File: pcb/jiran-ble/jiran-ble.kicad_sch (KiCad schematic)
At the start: 167 parts, among them J1 BATT, J2 USB-C Connector, J3 SWD, J4 BATT, J5 USB-C Connector, J6 SWD, Q1 SI2301CDS-T1-GE3, Q2 SI2301CDS-T1-GE3, SW1 SW_DPDT_x2, SW10 SW_Push, SW11 SW_Push, SW12 SW_Push, SW13 SW_Push, SW14 SW_Push, SW15 SW_Push, SW16 SW_Push, SW17 SW_Push, SW18 SW_Push, SW19 SW_Push, SW2 SW_Push, SW20 SW_Push, SW21 SW_Push, SW22 SW_Push, SW23 SW_Push, SW24 SW_Push, SW25 SW_Push, SW26 SW_Push, SW27 SW_Push, SW28 SW_Push, SW29 SW_Push, SW3 SW_Push, SW30 SW_Push, SW31 SW_Push, SW32 SW_Push, SW33 SW_Push, SW34 SW_Push, SW35 SW_Push, SW36 SW_Push, SW37 SW_Push, SW38 SW_Push, SW39 SW_Push, SW4 SW_Push, SW40 SW_Push, SW41 SW_Push, SW42 SW_Push, SW43 SW_Push, SW44 SW_Push, SW45 SW_Push, SW46 SW_Push, SW47 SW_Push, SW48 SW_Push, SW49 SW_Push, SW5 SW_Push, SW50 SW_Push, SW51 SW_Push, SW52 SW_Push, SW53 SW_Push, SW54 SW_Push, SW55 SW_Push, SW56 SW_Push, SW57 SW_Push, SW58 SW_Push, SW59 SW_Push, SW6 SW_Push, SW7 SW_Push, SW8 SW_Push, SW9 SW_Push, U1 HOLYIOT-18010-NRF52840_simple, U2 XC6220B331MR-G, U3 TP4054, U4 HOLYIOT-18010-NRF52840_simple, U5 XC6220B331MR-G, U6 TP4054

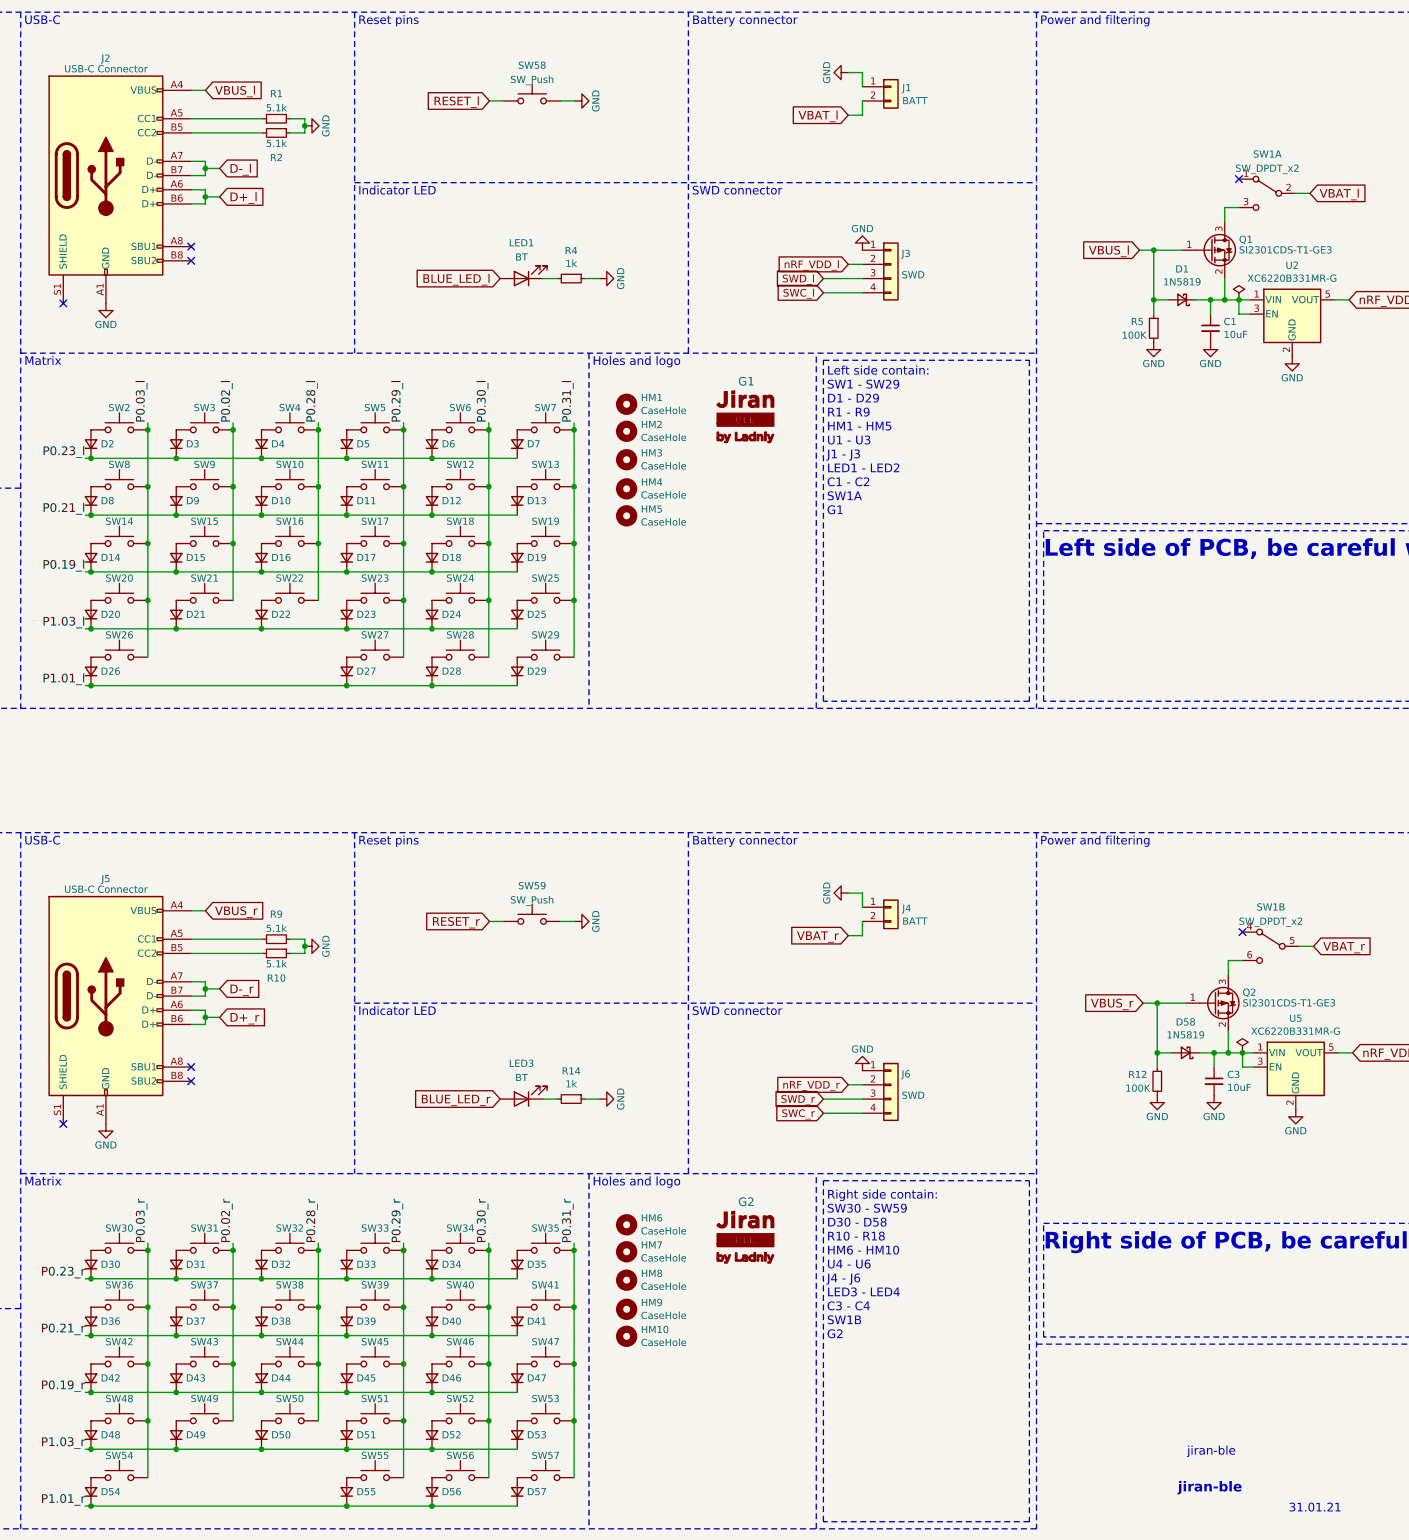
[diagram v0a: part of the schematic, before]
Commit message: Change DPDT symbol
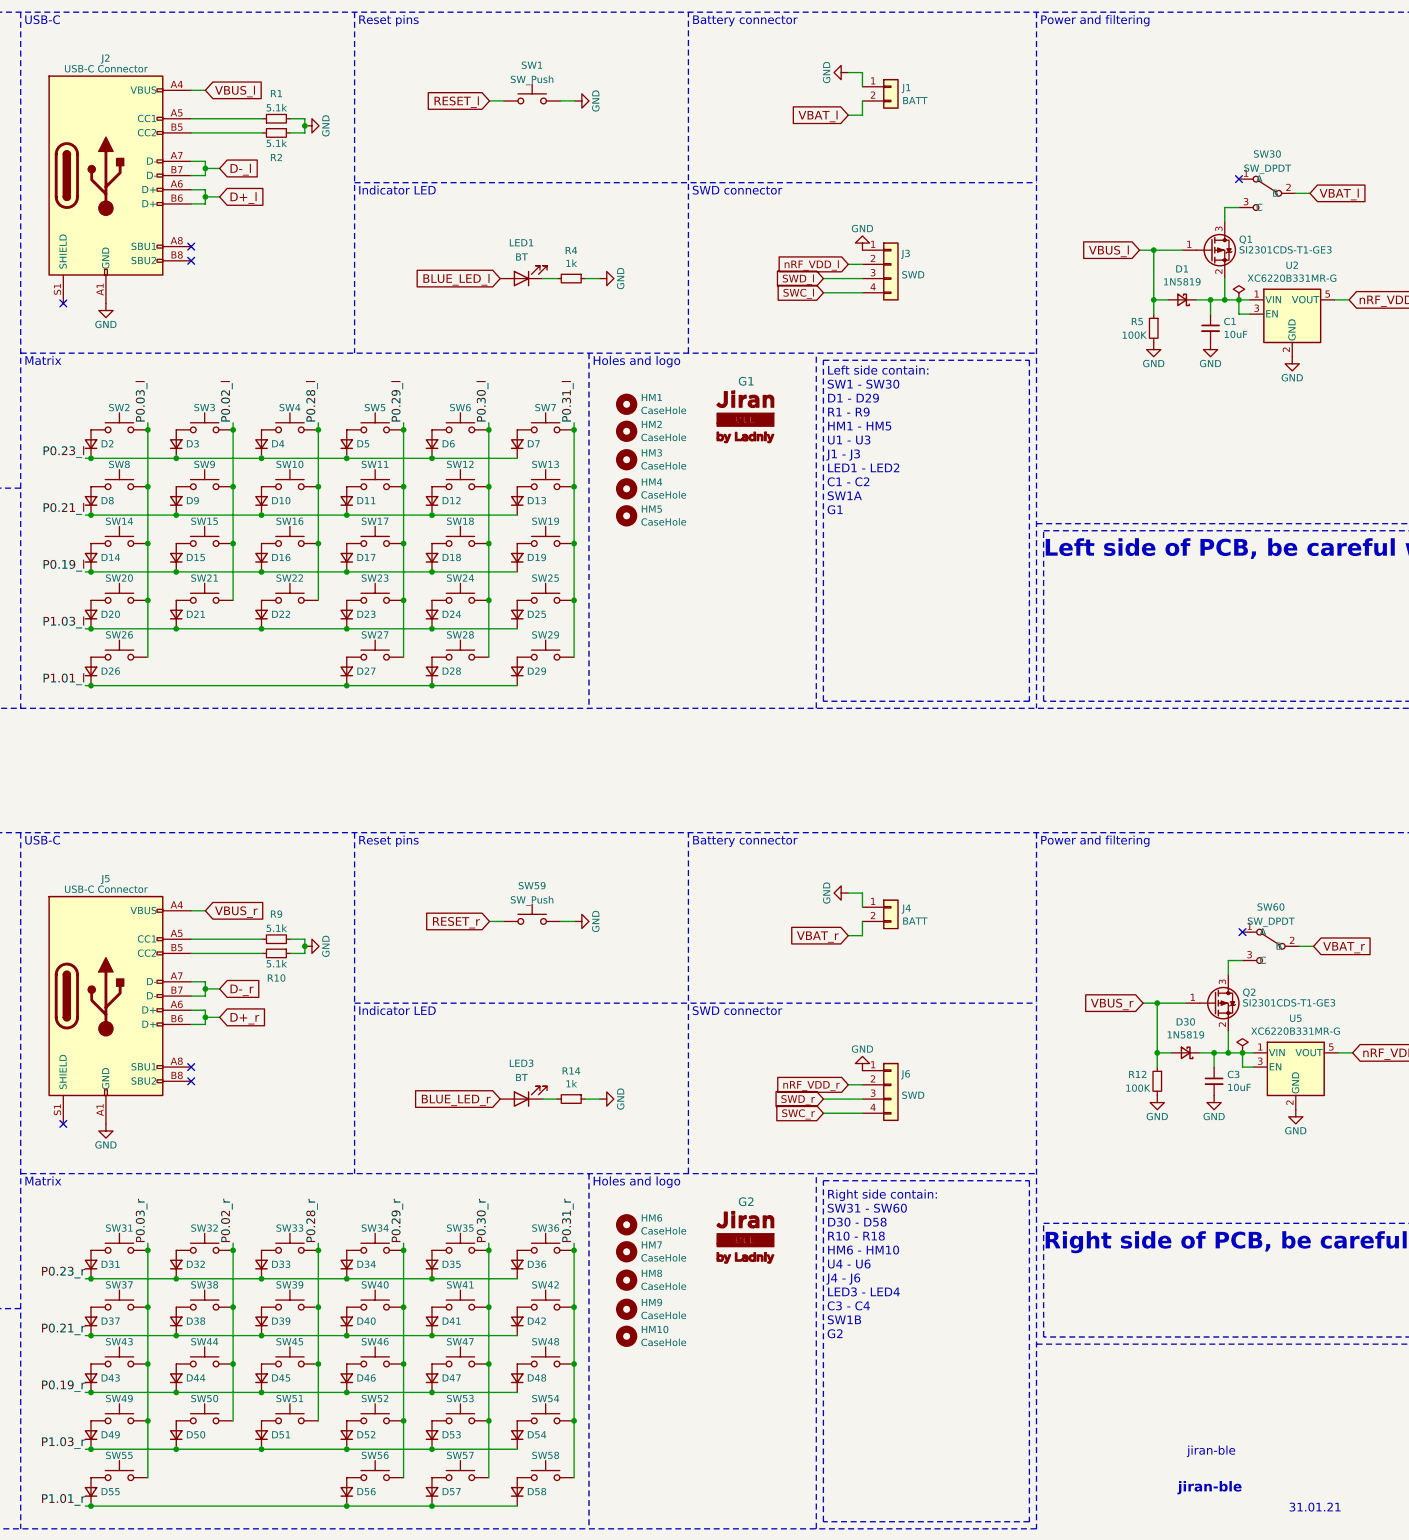
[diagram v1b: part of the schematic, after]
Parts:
- removed SW1: SW_DPDT_x2, jiran-ble:Switch_SMD_MSK-12C02, symbol Switch:SW_DPDT_x2
- added SW30, SW60: SW_DPDT, symbol jiran-ble-new:SW_DPDT
- renumbered D58 to D30, D30 to D31, D31 to D32, D32 to D33, D33 to D34, D34 to D35, D35 to D36, D36 to D37, D37 to D38, D38 to D39, D39 to D40, D40 to D41, D41 to D42, D42 to D43, D43 to D44, D44 to D45, D45 to D46, D46 to D47, D47 to D48, D48 to D49, D49 to D50, D50 to D51, D51 to D52, D52 to D53, D53 to D54, D54 to D55, D55 to D56, D56 to D57, D57 to D58, SW58 to SW1, SW30 to SW31, SW31 to SW32, SW32 to SW33, SW33 to SW34, SW34 to SW35, SW35 to SW36, SW36 to SW37, SW37 to SW38, SW38 to SW39, SW39 to SW40, SW40 to SW41, SW41 to SW42, SW42 to SW43, SW43 to SW44, SW44 to SW45, SW45 to SW46, SW46 to SW47, SW47 to SW48, SW48 to SW49, SW49 to SW50, SW50 to SW51, SW51 to SW52, SW52 to SW53, SW53 to SW54, SW54 to SW55, SW55 to SW56, SW56 to SW57, SW57 to SW58
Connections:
- net VBAT_l: now also SW30.2 (B)
- net VBAT_r: now also SW60.2 (B)
- net at Q1.3 (D): now also SW30.3 (C)
- net at Q2.3 (D): now also SW60.3 (C)
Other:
- note added: "Left side contain: SW1 - SW30 D1 - D29 R1 - R9 HM1 - HM5 U1 - U3 J1 - J3 LED1 - LED2 C1 - C2 SW1A G1"
- note added: "Right side contain: SW31 - SW60 D30 - D58 R10 - R18 HM6 - HM10 U4 - U6 J4 - J6 LED3 - LED4 C3 - C4 SW1B G2"
- note removed: "Left side contain: SW1 - SW29 D1 - D29 R1 - R9 HM1 - HM5 U1 - U3 J1 - J3 LED1 - LED2 C1 - C2 SW1A G1"
- note removed: "Right side contain: SW30 - SW59 D30 - D58 R10 - R18 HM6 - HM10 U4 - U6 J4 - J6 LED3 - LED4 C3 - C4 SW1B G2"

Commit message: Assign DPDT footprints
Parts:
- SW30, SW60: footprint (none) -> jiran-ble:MSK-12C02
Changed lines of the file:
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@@
     (property "Reference" "SW30" (id 0) (at 325.755 38.1 0))
     (property "Value" "SW_DPDT" (id 1) (at 325.755 40.64 0))
-    (property "Footprint" "" (id 2) (at 323.85 37.465 0)
+    (property "Footprint" "jiran-ble:MSK-12C02" (id 2) (at 323.85 37.465 0)
       (effects (font (size 1.27 1.27)) hide)
     )
@@
     (property "Reference" "SW60" (id 0) (at 326.39 172.72 0))
     (property "Value" "SW_DPDT" (id 1) (at 326.39 175.26 0))
-    (property "Footprint" "" (id 2) (at 324.485 172.085 0)
+    (property "Footprint" "jiran-ble:MSK-12C02" (id 2) (at 324.485 172.085 0)
       (effects (font (size 1.27 1.27)) hide)
     )
@@
     )
     (path "/db325e92-5360-45ed-9c6f-d56c57cf171b"
-      (reference "SW30") (unit 1) (value "SW_DPDT") (footprint "")
+      (reference "SW30") (unit 1) (value "SW_DPDT") (footprint "jiran-ble:MSK-12C02")
     )
     (path "/00000000-0000-0000-0000-00006130bef7"
@@
     )
     (path "/a6d535f7-c651-49c0-a33d-9ae4aaa71f84"
-      (reference "SW60") (unit 1) (value "SW_DPDT") (footprint "")
+      (reference "SW60") (unit 1) (value "SW_DPDT") (footprint "jiran-ble:MSK-12C02")
     )
     (path "/00000000-0000-0000-0000-00006068c8f8"

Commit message: Backups update, autosave
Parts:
- removed G1, G2: logo-jiran-hotswap, jiran-ble:logotype, symbol jiran-ble:jiran-ble
- removed J2, J5: USB-C Connector, jiran-ble:USB-C-31-M-27, symbol nrfmicro-rescue:USB_C_Receptacle_USB2.0-Connector
- removed SW30, SW60: SW_DPDT, jiran-ble:MSK-12C02, symbol jiran-ble-new:SW_DPDT
- removed U1, U4: HOLYIOT-18010-NRF52840_simple, jiran-ble:Holyiot-18010-nRF52840, symbol jiran-ble:HOLYIOT-18010-NRF52840_simple
- removed U2, U5: XC6220B331MR-G, jiran-ble:SOT-23-5, symbol nrfmicro-rescue:AP2112K-3.3-Regulator_Linear
- added G1, G2: Logo-Jiran-BLE, jiran-ble:logotype, symbol jiran-ble:Logo-Jiran-BLE
- added J2, J5: USB-C-Receptacle, jiran-ble:USB-C-31-M-27, symbol jiran-ble:USB-C-Receptacle
- added SW30, SW60: SW_DPDT, jiran-ble:MSK-12C02, symbol jiran-ble:SW_DPDT
- added U1, U4: HOLYIOT-18010-NRF52840_Simple, jiran-ble:Holyiot-18010-nRF52840, symbol jiran-ble:HOLYIOT-18010-NRF52840_Simple
- added U2, U5: AP2112K-3.3, jiran-ble:SOT-23-5, symbol jiran-ble:AP2112K-3.3
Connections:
- net BATTERY_PIN_l: now also U1.12 (P0.04/AIN2)
- net BATTERY_PIN_r: now also U4.12 (P0.04/AIN2)
- net BLUE_LED_l: now also U1.3 (P1.10)
- net BLUE_LED_r: now also U4.3 (P1.10)
- net D+_l: now also J2.A6 (D+), J2.B6 (D+), U1.24 (USB_D+)
- net D+_r: now also J5.A6 (D+), J5.B6 (D+), U4.24 (USB_D+)
- net D-_l: now also J2.A7 (D-), J2.B7 (D-), U1.23 (USB_D-)
- net D-_r: now also J5.A7 (D-), J5.B7 (D-), U4.23 (USB_D-)
- net GND: now also J2.A1 (GND), J2.A12 (GND), J2.B1 (GND), J2.B12 (GND), J5.A1 (GND), J5.A12 (GND), J5.B1 (GND), J5.B12 (GND), U1.1 (GND), U1.25 (GND), U1.37 (GND), U2.2 (GND), U4.1 (GND), U4.25 (GND), U4.37 (GND), U5.2 (GND)
- net P0.02_l: now also U1.7 (P0.02/AIN0)
- net P0.02_r: now also U4.7 (P0.02/AIN0)
- net P0.03_l: now also U1.6 (P0.03/AIN1)
- net P0.03_r: now also U4.6 (P0.03/AIN1)
- net P0.19_l: now also U1.20 (P0.19)
- net P0.19_r: now also U4.20 (P0.19)
- net P0.21_l: now also U1.19 (P0.21)
- net P0.21_r: now also U4.19 (P0.21)
- net P0.23_l: now also U1.18 (P0.23)
- net P0.23_r: now also U4.18 (P0.23)
- net P0.28_l: now also U1.8 (P0.28/AIN4)
- net P0.28_r: now also U4.8 (P0.28/AIN4)
- net P0.29_l: now also U1.9 (P0.29/AIN5)
- net P0.29_r: now also U4.9 (P0.29/AIN5)
- net P0.30_l: now also U1.10 (P0.30/AIN6)
- net P0.30_r: now also U4.10 (P0.30/AIN6)
- net P0.31_l: now also U1.11 (P0.31/AIN7)
- net P0.31_r: now also U4.11 (P0.31/AIN7)
- net P1.01_l: now also U1.29 (P1.01)
- net P1.01_r: now also U4.29 (P1.01)
- net P1.03_l: now also U1.28 (P1.03)
- net P1.03_r: now also U4.28 (P1.03)
- net RESET_l: now also U1.21 (P0.18/RESET)
- net RESET_r: now also U4.21 (P0.18/RESET)
- net SWC_l: now also U1.31 (SWDCLK)
- net SWC_r: now also U4.31 (SWDCLK)
- net SWD_l: now also U1.32 (SWDIO)
- net SWD_r: now also U4.32 (SWDIO)
- net VBAT_l: now also SW30.2 (B)
- net VBAT_r: now also SW60.2 (B)
- net VBUS_l: now also J2.A4 (VBUS), J2.A9 (VBUS), J2.B4 (VBUS), J2.B9 (VBUS), U1.22 (VBUS)
- net VBUS_r: now also J5.A4 (VBUS), J5.A9 (VBUS), J5.B4 (VBUS), J5.B9 (VBUS), U4.22 (VBUS)
- net nRF_VDD_l: now also U1.14 (VDD), U2.5 (VOUT)
- net nRF_VDD_r: now also U4.14 (VDD), U5.5 (VOUT)
- net at C1.1, D1.1 (K), Q1.2 (S): now also U2.1 (VIN), U2.3 (EN)
- net at Q1.3 (D): now also SW30.3 (C)
- net at R1.1: now also J2.A5 (CC1)
- net at R2.2: now also J2.B5 (CC2)
- net at R9.1: now also J5.A5 (CC1)
- net at R10.2: now also J5.B5 (CC2)
- net at C3.1, D30.1 (K), Q2.2 (S): now also U5.1 (VIN), U5.3 (EN)
- net at Q2.3 (D): now also SW60.3 (C)
